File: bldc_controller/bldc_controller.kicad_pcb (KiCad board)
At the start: 6 copper layers, 69.8 x 76.7 mm, 232 parts, among them J1 XT60PW-M, J10 JST S2B-PH-SM4-TB, J11 Phase A, J12 Phase B, J13 Phase C, J2 XT60PW-M, J3 SM08B-GHS-TB, J4 SM07B-GHS-TB, J5 JST S2B-PH-SM4-TB, J6 SM06B-GHS-TB, J7 Nano-Fit 1x03, J8 Nano-Fit 1x03, J9 SM05B-GHS-TB, Q1 TPH2R408QM,L1Q, Q2 TPH2R408QM,L1Q, Q3 TPH2R408QM,L1Q, Q4 TPH2R408QM,L1Q, Q5 TPH2R408QM,L1Q, Q6 TPH2R408QM,L1Q, SW1 CAS-220TA, U1 SMBJ51CD-M3/H, U10 DRV8353FS, U11 SMBJ51CD-M3/H, U12 LMR36006FSCQRNXRQ1, U2 MAX15062BATA+T, U3 ADP5301ACBZ-4-R7, U4 LP2992IM5-3.3/NOPB, U5 STM32G474RET3, U6 AS5047P, U7 AS5048B, U8 SN65HVD35DR, U9 TCAN1051HGVDRBRQ1

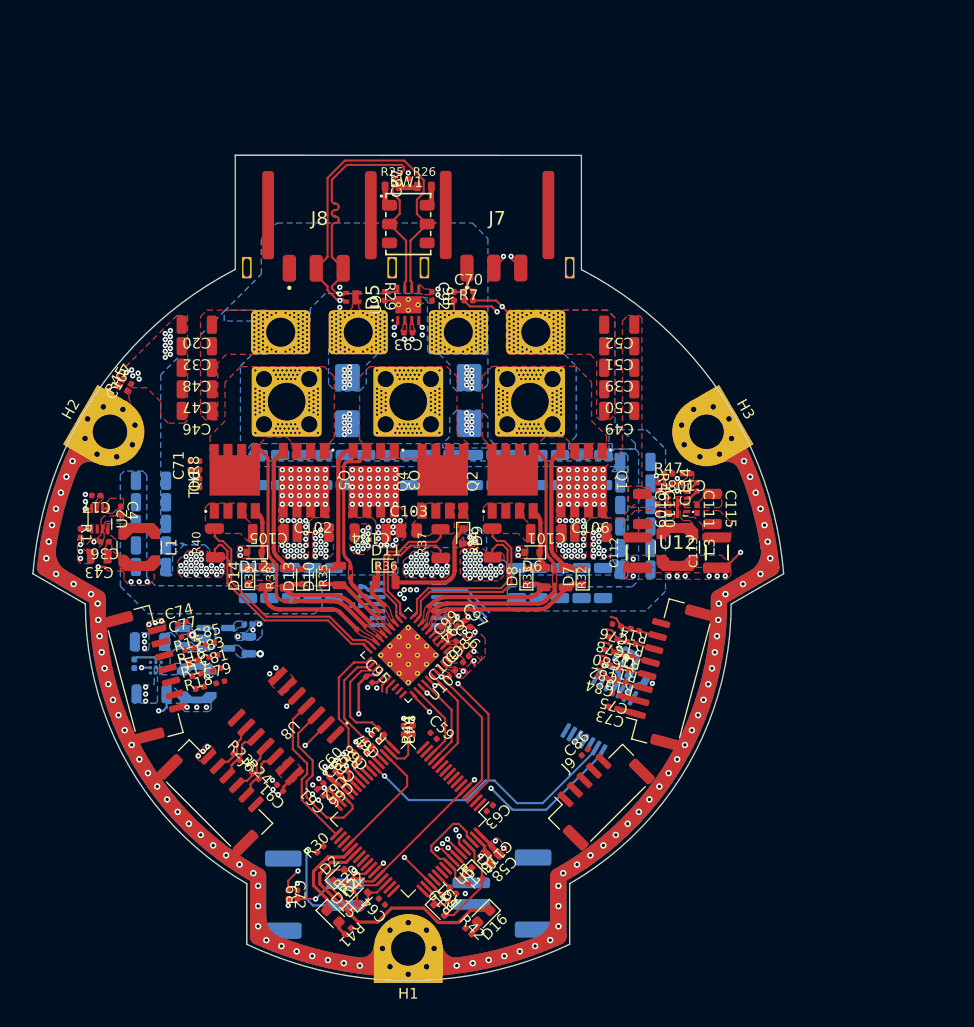
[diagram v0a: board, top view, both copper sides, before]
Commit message: Added TVS diodes to all interfaces
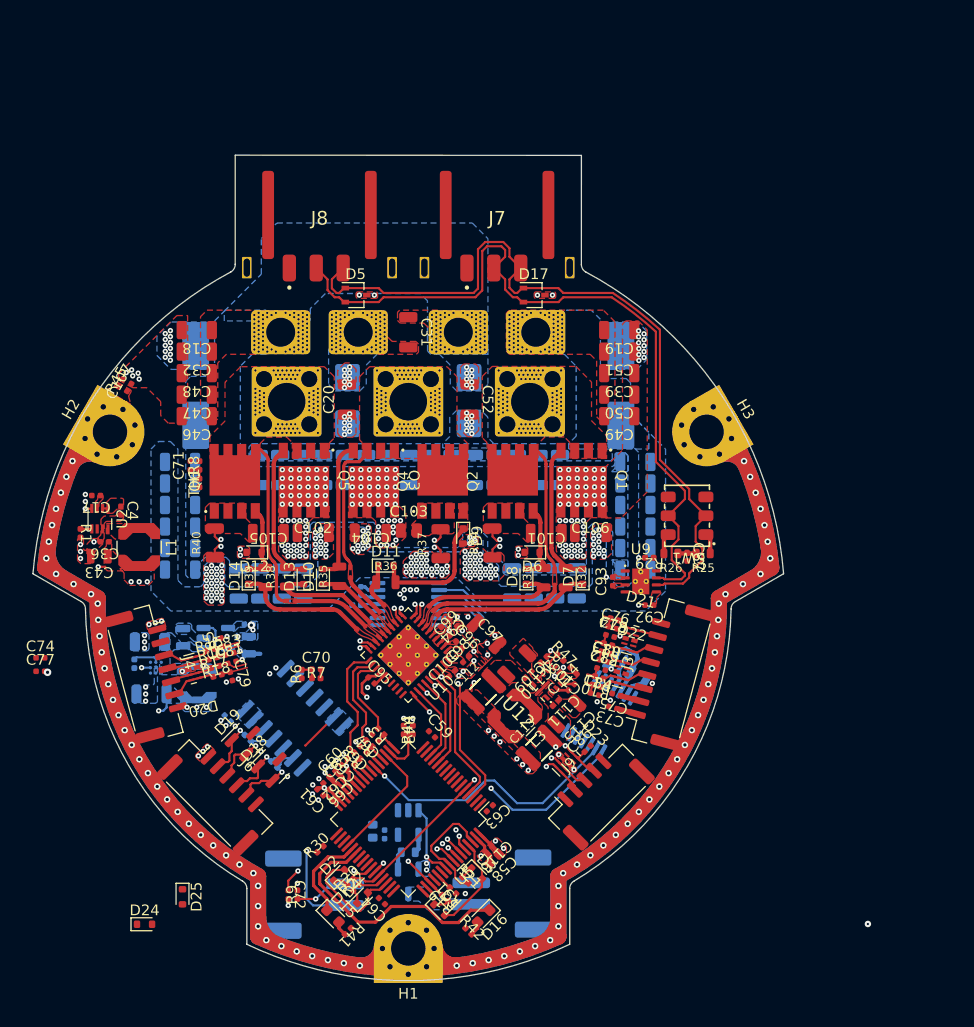
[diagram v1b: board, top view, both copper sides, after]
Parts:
- added C117: 47u 100V, Capacitor_SMD:CP_Elec_8x10.5, B.Cu at (169.7, 79.4)
- added C118: 47u 100V, Capacitor_SMD:CP_Elec_8x10.5, B.Cu at (130.2, 79.4)
- added C119: 100n, 0_capacitor_smd:C_0402_1005_DensityHigh, B.Cu at (147.7, 121.1)
- added C120: 4u7, 0_capacitor_smd:C_0603_1608_DensityHigh, B.Cu at (146.6, 120.8)
- added D17: PESD2CANFD24V-UX, Package_TO_SOT_SMD:SOT-323_SC-70, F.Cu at (161.6, 71.0)
- added D18: CDSOT23-SM712, Package_TO_SOT_SMD:SOT-23, F.Cu at (137.3, 114.8)
- added D19: CDSOT23-SM712, Package_TO_SOT_SMD:SOT-23, F.Cu at (134.8, 112.4)
- added D20: PESD4USB5B-TTSX, 0_package_DFN_QFN:DFN2510-D10, F.Cu at (129.9, 105.7)
- added D21: PESD4USB5B-TTSX, 0_package_DFN_QFN:DFN2510-D10, F.Cu at (170.5, 103.0)
- added D22: PESD4USB3U-TTSX, 0_package_DFN_QFN:DFN2510-D10, F.Cu at (169.7, 106.1)
- added D23: PESD4USB3U-TTSX, 0_package_DFN_QFN:DFN2510-D10, F.Cu at (164.6, 114.4)
- added D24: BAT41KFILM, Diode_SMD:D_SOD-523, F.Cu at (125.4, 129.4)
- added D25: BAT41KFILM, Diode_SMD:D_SOD-523, F.Cu at (128.9, 126.9)
- added Q7: SSM3K324R,LF, Package_TO_SOT_SMD:SOT-23-3, B.Cu at (149.9, 125.5)
- added R48: 10R, 0_resistor_smd:R_0603_1608_DensityHigh, B.Cu at (149.9, 122.8)
- added U13: DGD0216WT-7, Package_TO_SOT_SMD:TSOT-23-5, B.Cu at (149.9, 120.0)
- C18, C19, C31: moved to F.Cu
- C91, R23, R24, U8: moved to B.Cu
- C97: value 470n X7R 100V -> 4u7 100V; footprint 0_capacitor_smd:C_0402_1005_DensityHigh -> 0_capacitor_smd:C_1206_3216_DensityHighest
- D11: footprint 0_diode_smd:D_SOD-523_Spaced -> Diode_SMD:D_SOD-523
- D5: value PESD2CANFD27U-QCZ -> PESD2CANFD24V-UX; footprint 0_package_SOT_TO_SMD:SOT8009 -> Package_TO_SOT_SMD:SOT-323_SC-70
- moved R25 44.7 mm to (177.3, 95.0), turned to 180 degrees
- moved C87 43.3 mm to (175.8, 95.3), turned to -90 degrees
- moved R26 41.1 mm to (174.3, 95.0), turned to 180 degrees
- moved C18 38.0 mm to (130.2, 74.2), turned to 180 degrees
- moved R6 37.8 mm to (140.0, 106.2)
- moved C70 37.8 mm to (141.3, 105.8)
- moved R7 37.8 mm to (141.3, 106.6)
- moved SW1 37.5 mm to (175.8, 91.5), turned to 180 degrees
- moved C92 35.1 mm to (172.3, 99.8), turned to 180 degrees
- moved R29 34.6 mm to (172.3, 95.4), turned to 180 degrees
- moved U9 33.6 mm to (171.5, 97.6), turned to 0 degrees
- moved C93 29.9 mm to (168.9, 97.6), turned to 90 degrees
- moved C31 29.5 mm to (149.9, 74.5)
- moved NT2 26.9 mm to (155.8, 107.6), turned to -90 degrees
- moved C113 24.5 mm to (162.0, 113.1), turned to 45 degrees
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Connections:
- D5 pad 1: /FDCAN Transceiver/FDCAN_P -> /FDCAN Transceiver/FDCAN_N
- D5 pad 2: /FDCAN Transceiver/FDCAN_N -> /FDCAN Transceiver/FDCAN_P
- J10 pad 2: GND -> /Fan Control/FAN_SW
- J6 pad 2: /Interconnects/RS422_D+ -> /Interconnects/RS422_R+
- J6 pad 3: /Interconnects/RS422_D- -> /Interconnects/RS422_R-
- J6 pad 4: /Interconnects/RS422_R- -> /Interconnects/RS422_D-
- J6 pad 5: /Interconnects/RS422_R+ -> /Interconnects/RS422_D+
- J7 pad 2: /FDCAN Transceiver/FDCAN_N -> /FDCAN Transceiver/FDCAN_P
- J7 pad 3: /FDCAN Transceiver/FDCAN_P -> /FDCAN Transceiver/FDCAN_N
- J8 pad 2: /FDCAN Transceiver/FDCAN_N -> /FDCAN Transceiver/FDCAN_P
- J8 pad 3: /FDCAN Transceiver/FDCAN_P -> /FDCAN Transceiver/FDCAN_N
- R23 pad 1: /Interconnects/RS422_D+ -> /Interconnects/RS422_R+
- R23 pad 2: /Interconnects/RS422_D- -> /Interconnects/RS422_R-
- R24 pad 1: /Interconnects/RS422_R- -> /Interconnects/RS422_D-
- R24 pad 2: /Interconnects/RS422_R+ -> /Interconnects/RS422_D+
- SW1 pad 2: /FDCAN Transceiver/FDCAN_P -> /FDCAN Transceiver/FDCAN_N
- SW1 pad 5: /FDCAN Transceiver/FDCAN_N -> /FDCAN Transceiver/FDCAN_P
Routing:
- net /FDCAN Transceiver/FDCAN_RX: track 82.7 -> 1.18 mm, vias 2 -> 1
- net /FDCAN Transceiver/FDCAN_TX: track 80.9 -> 1.81 mm, vias 2 -> 1
- net /Microcontroller IO/SENSE_VBAT: track 80.7 -> 3.01 mm, vias 2 -> 1
- net /FDCAN Transceiver/FDCAN_P: track 57.2 -> 73.2 mm, vias 2 -> 0
- net /FDCAN Transceiver/FDCAN_N: track 57.9 -> 73.9 mm, vias 2 -> 0
- net /Microcontroller IO/RS422_~{RE}: track 15.9 -> 0.00 mm
- net /Microcontroller IO/RS422_DE: track 14.6 -> 0.00 mm
- net GND: track 25.0 -> 16.6 mm, vias 215 -> 234
- net /Microcontroller IO/FAN_CTRL: track 0.00 -> 6.86 mm, vias 0 -> 1
- net /Power Generation/FB_12V: track 15.9 -> 11.0 mm
- net /Interconnects/AUX2P_A: track 0.00 -> 4.37 mm
- net /Interconnects/AUX2P_D: track 0.00 -> 4.36 mm
- net /Interconnects/NRST: track 0.00 -> 4.19 mm, vias 0 -> 1
- net /Interconnects/AUX2P_C: track 0.00 -> 3.99 mm
- net /Interconnects/AUX2P_B: track 0.00 -> 3.98 mm
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- added copper zone on B.Cu, net /Fan Control/FAN_SW
- added copper zone on In4.Cu, net GND
- removed copper zone on In2.Cu, net /FDCAN Transceiver/FDCAN_RX
- removed copper zone on F.Cu, net /Motor Control/Three Phase Inverter/FET_GLC
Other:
- board size 69.8 x 76.7 mm -> 69.7 x 76.7 mm

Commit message: might have fixed net issue, added dxf and svgs
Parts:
- added C121: 330n, 0_capacitor_smd:C_0402_1005_DensityHigh, F.Cu at (149.5, 127.4)
- added C122: 330n, 0_capacitor_smd:C_0402_1005_DensityHigh, F.Cu at (176.2, 79.6)
- added R49: 100k, 0_resistor_smd:R_0402_1005_DensityHigh, F.Cu at (150.3, 127.4)
- added R50: 100k, 0_resistor_smd:R_0402_1005_DensityHigh, F.Cu at (176.9, 79.2)
- R23, R24: value 120R -> 100R
- moved C77 13.6 mm to (128.9, 102.7), turned to 15 degrees
- moved C74 13.3 mm to (128.6, 101.5), turned to 15 degrees
- moved D25 3.85 mm to (132.0, 129.2)
- moved C63 1.75 mm to (157.8, 117.0)
- moved C79 1.70 mm to (132.6, 107.9), turned to -165 degrees
- moved C85 1.70 mm to (131.1, 102.4), turned to -165 degrees
- moved C83 1.63 mm to (131.7, 104.8), turned to -165 degrees
- moved C81 1.63 mm to (132.0, 105.5), turned to -165 degrees
- moved C116 1.50 mm to (157.3, 120.9)
- moved C58 1.50 mm to (157.9, 121.8)
- moved C60 1.50 mm to (143.4, 113.4)
- moved C61 1.50 mm to (141.7, 115.7)
- moved C62 1.50 mm to (142.3, 114.6)
- moved C64 1.50 mm to (147.4, 125.8)
- moved C65 1.50 mm to (144.0, 114.0)
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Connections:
- net /FDCAN Transceiver/FDCAN_N renamed /Project Architecture/Interface - FD-CAN/FDCAN_N
- net /FDCAN Transceiver/FDCAN_P renamed /Project Architecture/Interface - FD-CAN/FDCAN_P
- net /FDCAN Transceiver/FDCAN_RX renamed /Project Architecture/Interface - FD-CAN/FDCAN_RX
- net /FDCAN Transceiver/FDCAN_S renamed /Project Architecture/Interface - FD-CAN/FDCAN_S
- net /FDCAN Transceiver/FDCAN_TX renamed /Project Architecture/Interface - FD-CAN/FDCAN_TX
- net /Fan Control/FAN_GATE renamed /Project Architecture/Interface - Fan Control/FAN_GATE
- net /Fan Control/FAN_OUT renamed /Project Architecture/Interface - Fan Control/FAN_OUT
- net /Fan Control/FAN_SW renamed /Project Architecture/Interface - Fan Control/FAN_SW
- net /Fan Control/FAN_~{IN} renamed /Project Architecture/Interface - Fan Control/FAN_~{IN}
- net /Interconnects/AUX1P_A renamed /Project Architecture/Interface - Interconnects/AUX1P_A
- net /Interconnects/AUX1P_B renamed /Project Architecture/Interface - Interconnects/AUX1P_B
- net /Interconnects/AUX1P_C renamed /Project Architecture/Interface - Interconnects/AUX1P_C
- net /Interconnects/AUX1P_D renamed /Project Architecture/Interface - Interconnects/AUX1P_D
- net /Interconnects/AUX1P_E renamed /Project Architecture/Interface - Interconnects/AUX1P_E
- net /Interconnects/AUX1_A renamed /Project Architecture/Interface - Interconnects/AUX1_A
- net /Interconnects/AUX1_B renamed /Project Architecture/Interface - Interconnects/AUX1_B
- net /Interconnects/AUX1_C renamed /Project Architecture/Interface - Interconnects/AUX1_C
- net /Interconnects/AUX1_D renamed /Project Architecture/Interface - Interconnects/AUX1_D
- net /Interconnects/AUX1_D_K renamed /Project Architecture/Interface - Interconnects/AUX1_D_K
- net /Interconnects/AUX1_E renamed /Project Architecture/Interface - Interconnects/AUX1_E
- net /Interconnects/AUX1_E_K renamed /Project Architecture/Interface - Interconnects/AUX1_E_K
- net /Interconnects/AUX1_I2C_PULLUP renamed /Project Architecture/Interface - Interconnects/AUX1_I2C_PULLUP
- net /Interconnects/AUX2P_A renamed /Project Architecture/Interface - Interconnects/AUX2P_A
- net /Interconnects/AUX2P_B renamed /Project Architecture/Interface - Interconnects/AUX2P_B
- net /Interconnects/AUX2P_C renamed /Project Architecture/Interface - Interconnects/AUX2P_C
- net /Interconnects/AUX2P_D renamed /Project Architecture/Interface - Interconnects/AUX2P_D
- net /Interconnects/AUX2_A renamed /Project Architecture/Interface - Interconnects/AUX2_A
- net /Interconnects/AUX2_B renamed /Project Architecture/Interface - Interconnects/AUX2_B
- net /Interconnects/AUX2_B_K renamed /Project Architecture/Interface - Interconnects/AUX2_B_K
- net /Interconnects/AUX2_C renamed /Project Architecture/Interface - Interconnects/AUX2_C
- net /Interconnects/AUX2_C_K renamed /Project Architecture/Interface - Interconnects/AUX2_C_K
- net /Interconnects/AUX2_D renamed /Project Architecture/Interface - Interconnects/AUX2_D
- net /Interconnects/AUX2_I2C_PULLUP renamed /Project Architecture/Interface - Interconnects/AUX2_I2C_PULLUP
- net /Interconnects/CAN_TERM_B renamed /Project Architecture/Interface - Interconnects/CAN_TERM_B
- net /Interconnects/CAN_TERM_MID renamed /Project Architecture/Interface - Interconnects/CAN_TERM_MID
- net /Interconnects/CAN_TERM_T renamed /Project Architecture/Interface - Interconnects/CAN_TERM_T
- net /Interconnects/NRST renamed /Project Architecture/Interface - Interconnects/NRST
- net /Interconnects/NTC_MOT_H renamed /Project Architecture/Interface - Interconnects/NTC_MOT_H
- net /Interconnects/NTC_MOT_L renamed /Project Architecture/Interface - Interconnects/NTC_MOT_L
- net /Interconnects/POS_SENSOR_CS renamed /Project Architecture/Interface - Interconnects/POS_SENSOR_CS
- net /Interconnects/RS422_D+ renamed /Project Architecture/Interface - Interconnects/RS422_D+
- net /Interconnects/RS422_D- renamed /Project Architecture/Interface - Interconnects/RS422_D-
- net /Interconnects/RS422_R+ renamed /Project Architecture/Interface - Interconnects/RS422_R+
- net /Interconnects/RS422_R- renamed /Project Architecture/Interface - Interconnects/RS422_R-
- net /Interconnects/SWCLK renamed /Project Architecture/Interface - Interconnects/SWCLK
- net /Interconnects/SWDIO renamed /Project Architecture/Interface - Interconnects/SWDIO
- net /LED Indicators/LED1 renamed /Project Architecture/MCU - IO/LED1
- net /LED Indicators/LED1_A renamed /Project Architecture/User - LED Indicators/LED1_A
- net /LED Indicators/LED2 renamed /Project Architecture/MCU - IO/LED2
- net /LED Indicators/LED2_A renamed /Project Architecture/User - LED Indicators/LED2_A
- net /Microcontroller IO/BOARD_VERSION renamed /Project Architecture/MCU - IO/BOARD_VERSION
- net /Microcontroller IO/DRV_CS renamed /Project Architecture/MCU - IO/DRV_CS
- net /Microcontroller IO/DRV_MISO renamed /Project Architecture/MCU - IO/DRV_MISO
- net /Microcontroller IO/DRV_MOSI renamed /Project Architecture/MCU - IO/DRV_MOSI
- net /Microcontroller IO/DRV_SCLK renamed /Project Architecture/MCU - IO/DRV_SCLK
- net /Microcontroller IO/FAN_CTRL renamed /Project Architecture/MCU - IO/FAN_CTRL
- net /Microcontroller IO/FILTER_SOA renamed /Project Architecture/MCU - IO/FILTER_SOA
- net /Microcontroller IO/FILTER_SOB renamed /Project Architecture/MCU - IO/FILTER_SOB
- net /Microcontroller IO/FILTER_SOC renamed /Project Architecture/MCU - IO/FILTER_SOC
- net /Microcontroller IO/MOTOR_ENABLE renamed /Project Architecture/MCU - IO/MOTOR_ENABLE
- net /Microcontroller IO/MOTOR_FAULT renamed /Project Architecture/MCU - IO/MOTOR_FAULT
- net /Microcontroller IO/MOTOR_HIZ renamed /Project Architecture/MCU - IO/MOTOR_HIZ
- net /Microcontroller IO/PWM_PHASEA renamed /Project Architecture/MCU - IO/PWM_PHASEA
- net /Microcontroller IO/PWM_PHASEB renamed /Project Architecture/MCU - IO/PWM_PHASEB
- net /Microcontroller IO/PWM_PHASEC renamed /Project Architecture/MCU - IO/PWM_PHASEC
- net /Microcontroller IO/RS422_DE renamed /Project Architecture/Interface - RS-422/RS422_DE
- net /Microcontroller IO/RS422_~{RE} renamed /Project Architecture/Interface - RS-422/RS422_~{RE}
- net /Microcontroller IO/SENSE_TEMP_FET renamed /Project Architecture/MCU - IO/SENSE_TEMP_FET
- net /Microcontroller IO/SENSE_TEMP_MOT renamed /Project Architecture/MCU - IO/SENSE_TEMP_MOT
- net /Microcontroller IO/SENSE_VBAT renamed /Project Architecture/MCU - IO/SENSE_VBAT
- net /Microcontroller IO/SOA renamed /Project Architecture/MCU - IO/SOA
- net /Microcontroller IO/SOB renamed /Project Architecture/MCU - IO/SOB
- net /Microcontroller IO/SOC renamed /Project Architecture/MCU - IO/SOC
- net /Motor Control/CPH renamed /Project Architecture/Motor Control - Top Level/CPH
- net /Motor Control/CPL renamed /Project Architecture/Motor Control - Top Level/CPL
- net /Motor Control/DVDD renamed /Project Architecture/Motor Control - Top Level/DVDD
- net /Motor Control/GHA renamed /Project Architecture/Motor Control - Top Level/GHA
- net /Motor Control/GHB renamed /Project Architecture/Motor Control - Top Level/GHB
- net /Motor Control/GHC renamed /Project Architecture/Motor Control - Top Level/GHC
- net /Motor Control/GLA renamed /Project Architecture/Motor Control - Top Level/GLA
- net /Motor Control/GLB renamed /Project Architecture/Motor Control - Top Level/GLB
- net /Motor Control/GLC renamed /Project Architecture/Motor Control - Top Level/GLC
- net /Motor Control/SA_N renamed /Project Architecture/Motor Control - Top Level/SA_N
- net /Motor Control/SA_P renamed /Project Architecture/Motor Control - Top Level/SA_P
- net /Motor Control/SB_N renamed /Project Architecture/Motor Control - Top Level/SB_N
- net /Motor Control/SB_P renamed /Project Architecture/Motor Control - Top Level/SB_P
- net /Motor Control/SC_N renamed /Project Architecture/Motor Control - Top Level/SC_N
- net /Motor Control/SC_P renamed /Project Architecture/Motor Control - Top Level/SC_P
- net /Motor Control/SHA renamed /Project Architecture/Motor Control - Top Level/SHA
- net /Motor Control/SHB renamed /Project Architecture/Motor Control - Top Level/SHB
- net /Motor Control/SHC renamed /Project Architecture/Motor Control - Top Level/SHC
- net /Motor Control/Three Phase Inverter/FET_GHA renamed /Project Architecture/Motor Control - Top Level/Motor Control - Inverter/FET_GHA
- net /Motor Control/Three Phase Inverter/FET_GHB renamed /Project Architecture/Motor Control - Top Level/Motor Control - Inverter/FET_GHB
- net /Motor Control/Three Phase Inverter/FET_GHC renamed /Project Architecture/Motor Control - Top Level/Motor Control - Inverter/FET_GHC
- net /Motor Control/Three Phase Inverter/FET_GLA renamed /Project Architecture/Motor Control - Top Level/Motor Control - Inverter/FET_GLA
- net /Motor Control/Three Phase Inverter/FET_GLB renamed /Project Architecture/Motor Control - Top Level/Motor Control - Inverter/FET_GLB
- net /Motor Control/Three Phase Inverter/FET_GLC renamed /Project Architecture/Motor Control - Top Level/Motor Control - Inverter/FET_GLC
- net /Motor Control/Three Phase Inverter/PHA renamed /Project Architecture/Motor Control - Top Level/Motor Control - Inverter/PHA
- net /Motor Control/Three Phase Inverter/PHB renamed /Project Architecture/Motor Control - Top Level/Motor Control - Inverter/PHB
- net /Motor Control/Three Phase Inverter/PHC renamed /Project Architecture/Motor Control - Top Level/Motor Control - Inverter/PHC
- net /Motor Control/Three Phase Inverter/SRC_LS_A renamed /Project Architecture/Motor Control - Top Level/Motor Control - Inverter/SRC_LS_A
- net /Motor Control/Three Phase Inverter/SRC_LS_B renamed /Project Architecture/Motor Control - Top Level/Motor Control - Inverter/SRC_LS_B
- net /Motor Control/Three Phase Inverter/SRC_LS_C renamed /Project Architecture/Motor Control - Top Level/Motor Control - Inverter/SRC_LS_C
- net /Motor Control/VCP renamed /Project Architecture/Motor Control - Top Level/VCP
- net /Motor Control/VGLS renamed /Project Architecture/Motor Control - Top Level/VGLS
- net /Position Sensors/COMM_VDD renamed /Project Architecture/Sensing - Position/COMM_VDD
- net /Position Sensors/DIS_VDD3V renamed /Project Architecture/Sensing - Position/DIS_VDD3V
- net /Power Generation/ADJ_A3V3 renamed /Project Architecture/Power - Generation/ADJ_A3V3
- net /Power Generation/BOOT_12V renamed /Project Architecture/Power - Generation/BOOT_12V
- net /Power Generation/FB_12V renamed /Project Architecture/Power - Generation/FB_12V
- net /Power Generation/FB_3V3 renamed /Project Architecture/Power - Generation/FB_3V3
- net /Power Generation/FB_5V renamed /Project Architecture/Power - Generation/FB_5V
- net /Power Generation/FB_DIV_12V renamed /Project Architecture/Power - Generation/FB_DIV_12V
- net /Power Generation/LX_5V renamed /Project Architecture/Power - Generation/LX_5V
- net /Power Generation/MODE_3V3 renamed /Project Architecture/Power - Generation/MODE_3V3
- net /Power Generation/MODE_5V renamed /Project Architecture/Power - Generation/MODE_5V
- net /Power Generation/PG_12V renamed /Project Architecture/Power - Generation/PG_12V
- net /Power Generation/PG_3V3 renamed /Project Architecture/Power - Generation/PG_3V3
- net /Power Generation/SW_12V renamed /Project Architecture/Power - Generation/SW_12V
- net /Power Generation/SW_3V3 renamed /Project Architecture/Power - Generation/SW_3V3
- net /Power Generation/VCC_12V renamed /Project Architecture/Power - Generation/VCC_12V
- net /Power Generation/VCC_5V renamed /Project Architecture/Power - Generation/VCC_5V
- net /Power Generation/VID_3V3 renamed /Project Architecture/Power - Generation/VID_3V3
- net /Power Generation/~{RST}_5V renamed /Project Architecture/Power - Generation/~{RST}_5V
- J4 pad MP: (no net) -> CHASSIS
- J9 pad MP: (no net) -> CHASSIS
- U5 pad 10: unconnected-(U5B-PC2-Pad10) -> /Project Architecture/MCU - IO/PC1
- U5 pad 11: unconnected-(U5B-PC3-Pad11) -> /Project Architecture/MCU - IO/PC3
- U5 pad 23: unconnected-(U5B-PC5-Pad23) -> /Project Architecture/MCU - IO/PC5
- U5 pad 39: unconnected-(U5B-PC7-Pad39) -> /Project Architecture/MCU - IO/PC7
- U5 pad 40: unconnected-(U5B-PC8-Pad40) -> /Project Architecture/MCU - IO/PC8
- U5 pad 41: unconnected-(U5B-PC9-Pad41) -> /Project Architecture/MCU - IO/PC9
- U5 pad 54: unconnected-(U5B-PC12-Pad54) -> /Project Architecture/MCU - IO/PC12
- U5 pad 8: unconnected-(U5B-PC0-Pad8) -> /Project Architecture/MCU - IO/PC0
- U5 pad 9: unconnected-(U5B-PC1-Pad9) -> /Project Architecture/MCU - IO/PC1
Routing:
- net CHASSIS: track 991.3 -> 0.00 mm
- net /Project Architecture/Interface - Interconnects/AUX2_A: track 2.28 -> 35.8 mm, vias 0 -> 2
- net /Project Architecture/Interface - Interconnects/AUX2_D: track 3.91 -> 33.4 mm, vias 1 -> 2
- net /Project Architecture/Interface - Interconnects/AUX1_E: track 12.7 -> 41.9 mm, vias 0 -> 2
- net /Project Architecture/Interface - Interconnects/AUX2_C: track 30.8 -> 54.8 mm, vias 1 -> 2
- net /Project Architecture/Interface - Interconnects/AUX2_B: track 33.3 -> 56.4 mm, vias 2 -> 3
- net /Project Architecture/Interface - Interconnects/SWCLK: track 3.92 -> 24.6 mm, vias 1 -> 2
- net /Project Architecture/Interface - Interconnects/SWDIO: track 3.94 -> 24.2 mm
- net /Project Architecture/Interface - Interconnects/NRST: track 4.19 -> 23.1 mm, vias 1 -> 3
- net /Project Architecture/Interface - RS-422/RS422_DE: track 0.00 -> 16.6 mm, vias 0 -> 1
- net /Project Architecture/Interface - RS-422/RS422_~{RE}: track 0.00 -> 13.5 mm, vias 0 -> 1
- net /Project Architecture/Interface - Interconnects/AUX1_C: track 5.40 -> 18.3 mm, vias 0 -> 1
- net GND: track 16.6 -> 29.0 mm, vias 234 -> 252
- net /Project Architecture/Interface - Interconnects/AUX1_B: track 8.38 -> 20.2 mm, vias 1 -> 2
- net /Project Architecture/MCU - IO/MOTOR_ENABLE: track 18.0 -> 12.3 mm
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- added copper zone on B.Cu, net CHASSIS
- added copper zone on In1.Cu, net CHASSIS
- added copper zone on In2.Cu, net CHASSIS
- added copper zone on In3.Cu, net CHASSIS
- added copper zone on In4.Cu, net CHASSIS
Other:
- outline, holes or cut-outs redrawn

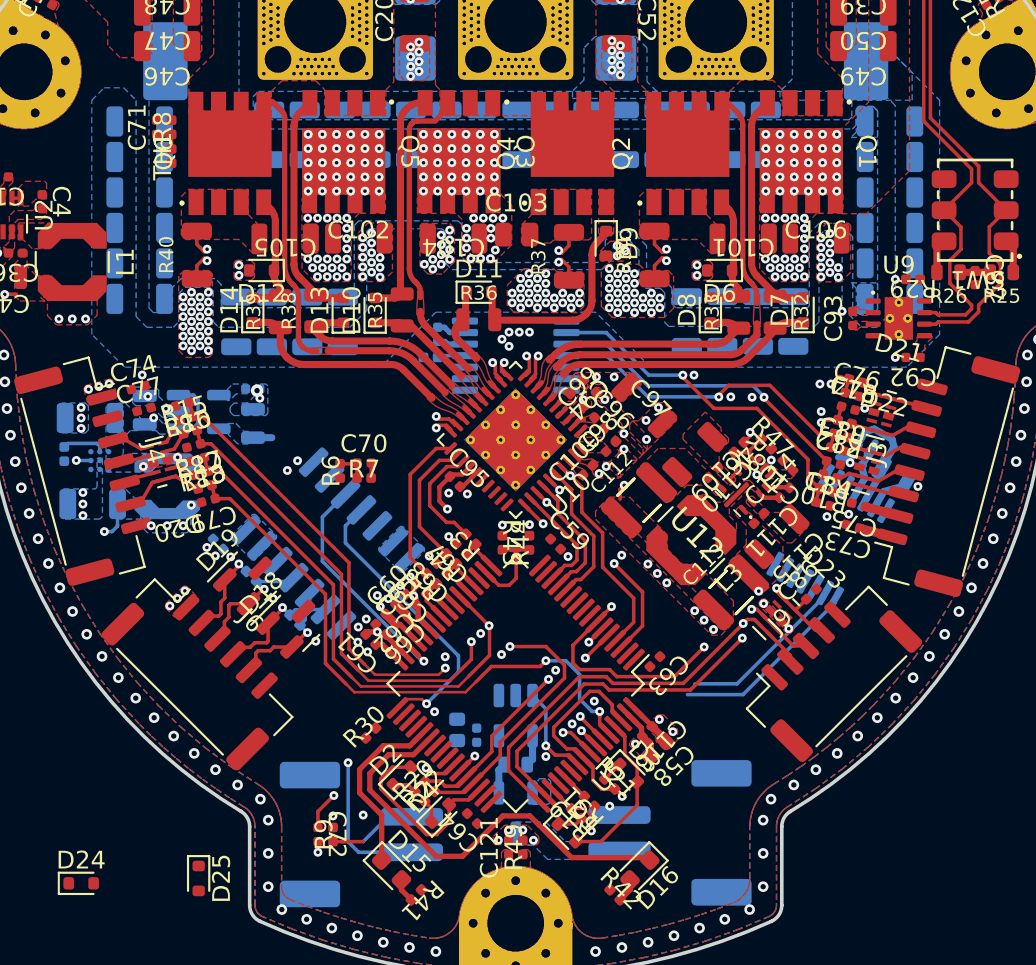
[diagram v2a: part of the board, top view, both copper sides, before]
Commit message: added chassis connection to connector MP. Might need to change design rules to be compatible with low-cost PCBWay
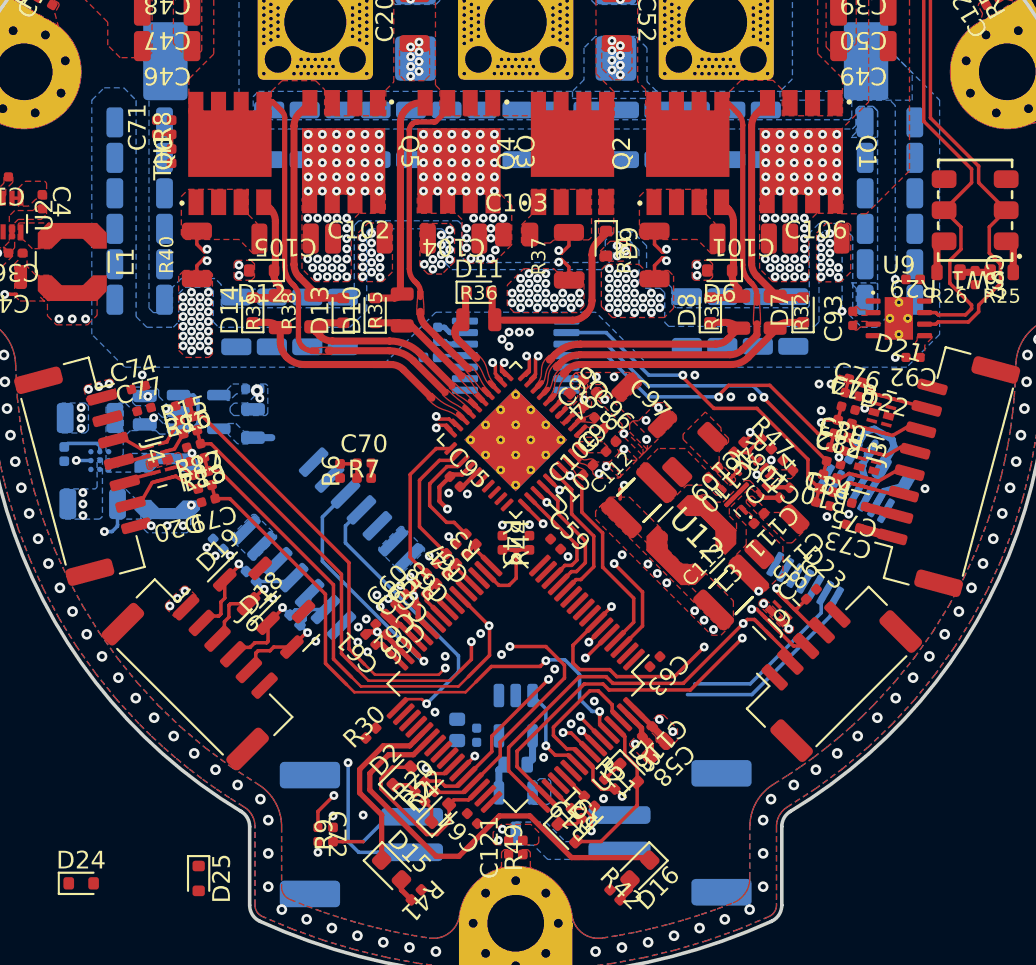
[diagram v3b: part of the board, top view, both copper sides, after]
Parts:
- moved NT9 0.06 mm to (145.6, 86.3)
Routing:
- net GND: track 29.0 -> 15.9 mm, vias 252 -> 247
